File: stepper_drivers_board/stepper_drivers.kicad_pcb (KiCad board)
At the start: 2 copper layers, 41.5 x 76.5 mm, 25 parts

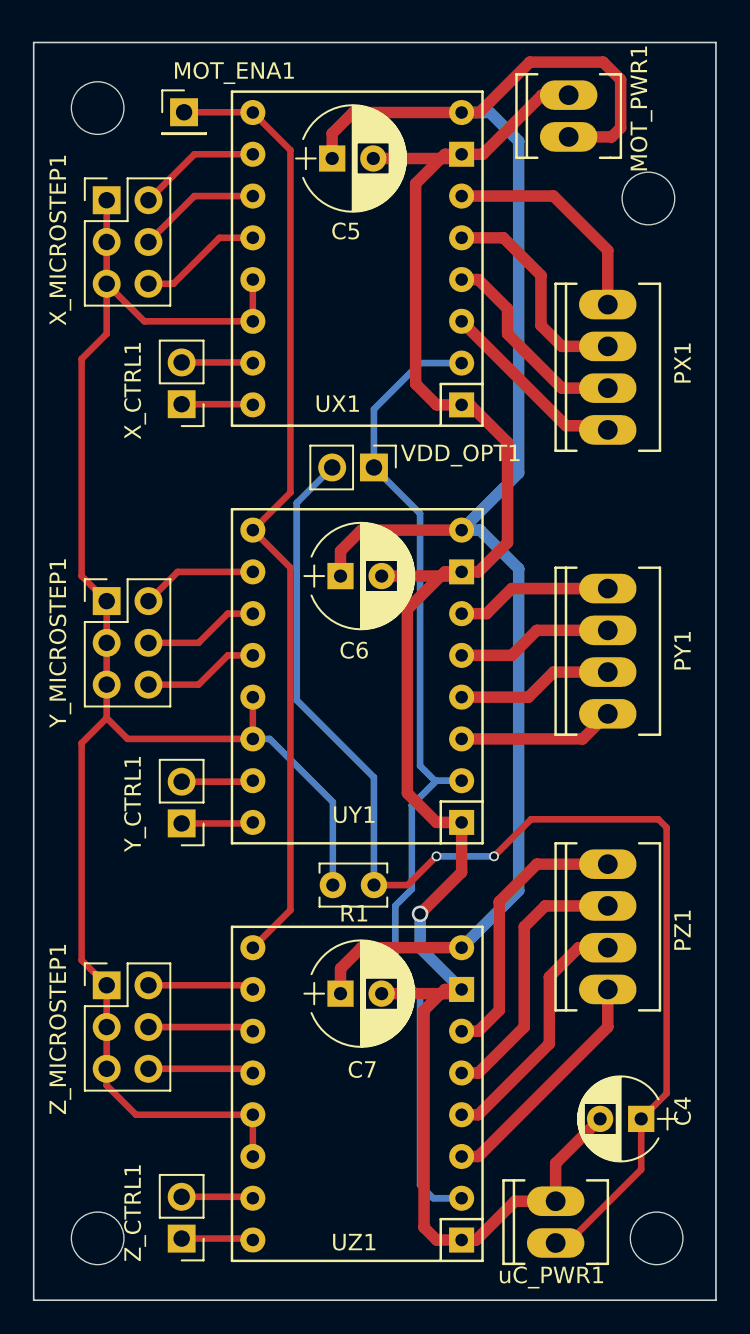
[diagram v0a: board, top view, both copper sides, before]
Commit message: minor board fixes: limit switches and stepper motors
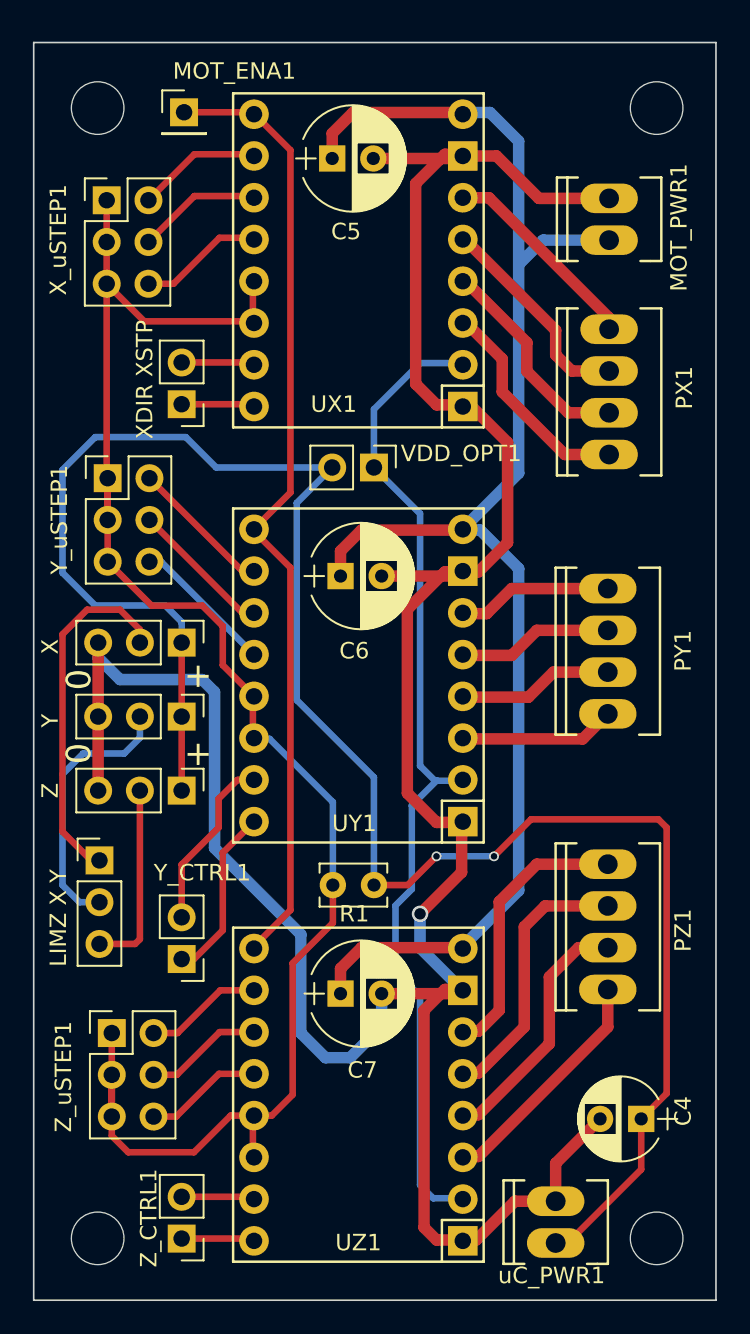
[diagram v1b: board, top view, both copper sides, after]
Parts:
- added LIMZ X Y: Conn_01x03, Pin_Headers:Pin_Header_Straight_1x03_Pitch2.54mm, F.Cu at (101.0, 91.0)
- added X: Conn_01x03, Pin_Headers:Pin_Header_Straight_1x03_Pitch2.54mm, F.Cu at (106.0, 77.8)
- added Y: Conn_01x03, Pin_Headers:Pin_Header_Straight_1x03_Pitch2.54mm, F.Cu at (106.0, 82.2)
- added Z: Conn_01x03, Pin_Headers:Pin_Header_Straight_1x03_Pitch2.54mm, F.Cu at (106.0, 86.8)
- XDIR XSTP: renamed from X_CTRL1
- moved Y_CTRL1 8.25 mm to (106.0, 97.0)
- moved Y_uSTEP1 7.48 mm to (101.5, 67.8)
- moved MOT_PWR1 6.74 mm to (132.0, 52.0)
- moved REF** 5.52 mm to (134.9, 45.2)
- moved Z_uSTEP1 2.92 mm to (101.8, 101.5)
- moved PX1 1.50 mm to (132.0, 62.5)
- moved UX1 0.12 mm to (116.8, 54.5)
- moved UZ1 0.09 mm to (116.8, 105.2)
- moved UY1 0.08 mm to (116.8, 79.8)
- renumbered X_MICROSTEP1 to X_uSTEP1, Y_MICROSTEP1 to Y_uSTEP1, Z_MICROSTEP1 to Z_uSTEP1
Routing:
- net GND: track 119.4 -> 170.5 mm
- net +5V: track 76.4 -> 119.4 mm
- net Net-(LIM1-Pad1): track 0.00 -> 21.6 mm
- net Net-(LIM1-Pad2): track 0.00 -> 16.3 mm
- net Net-(LIM1-Pad3): track 0.00 -> 11.6 mm
- net +12V: track 104.7 -> 93.1 mm
- net Net-(UY1-Pad15): track 4.36 -> 10.8 mm
- net Net-(UY1-Pad16): track 4.36 -> 10.6 mm
- net Net-(R1-Pad2): track 104.4 -> 102.6 mm
- net Net-(PX1-Pad1): track 11.6 -> 13.4 mm
- net Net-(UY1-Pad12): track 7.09 -> 8.70 mm
- net Net-(UY1-Pad10): track 7.09 -> 8.70 mm
- net Net-(UY1-Pad11): track 7.09 -> 8.70 mm
- net Net-(UZ1-Pad11): track 6.46 -> 7.55 mm
- net Net-(UZ1-Pad12): track 6.46 -> 7.55 mm
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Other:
- board text added: "+"
- board text added: "0"
